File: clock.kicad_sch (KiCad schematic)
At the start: 52 parts, among them J1 USB_C_Receptacle_USB2.0_16P, J3 Conn_01x02_Pin, J4 Conn_01x02_Pin, J5 Battery, Q1 2N7002K, Q2 NPN, SW1 SW_SPST, SW2 SW_SPST, SW4 SW_SPDT, SW5 SW_SPST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

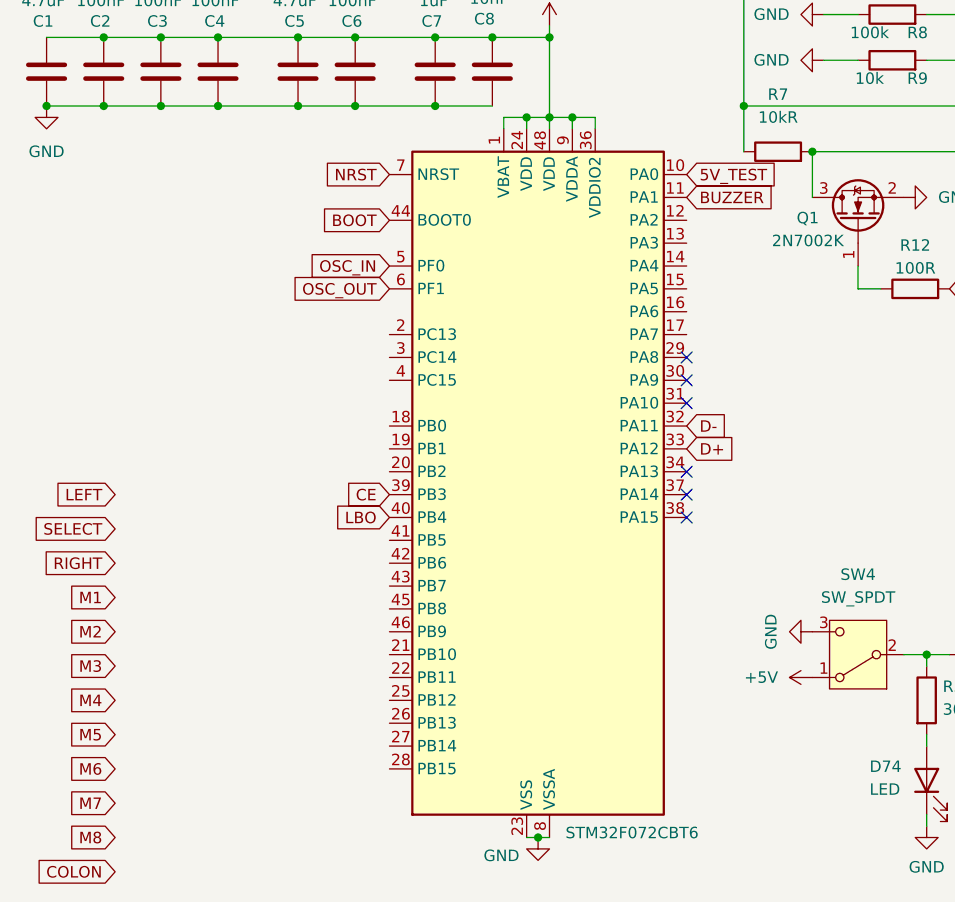
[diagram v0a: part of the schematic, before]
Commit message: all wiring done, need to clean up silk screen edge clips + double check pins for charlieplex & buttons
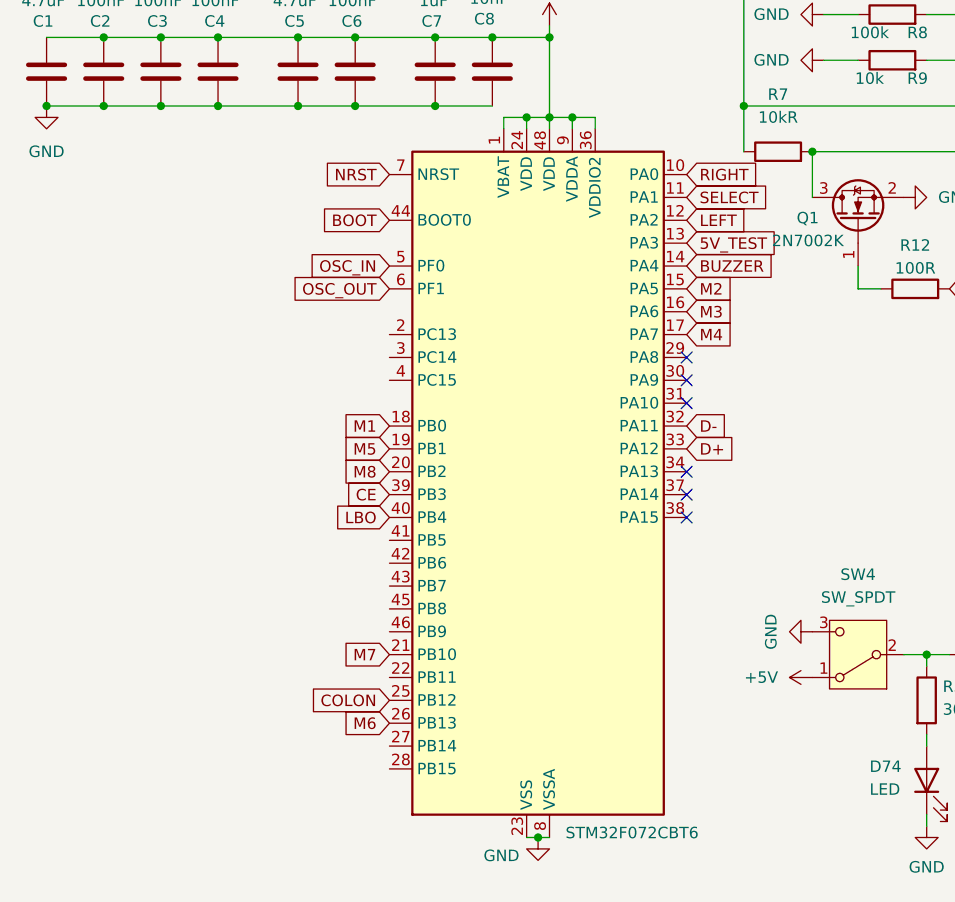
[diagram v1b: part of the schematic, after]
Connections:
- net 5V_TEST: now also U1.13 (PA3); no longer U1.10 (PA0)
- net BUZZER: now also U1.14 (PA4); no longer U1.11 (PA1)
- net COLON: now also U1.25 (PB12)
- net LEFT: now also U1.12 (PA2)
- net M1: now also U1.18 (PB0)
- net M2: now also U1.15 (PA5)
- net M3: now also U1.16 (PA6)
- net M4: now also U1.17 (PA7)
- net M5: now also U1.19 (PB1)
- net M6: now also U1.26 (PB13)
- net M7: now also U1.21 (PB10)
- net M8: now also U1.20 (PB2)
- net RIGHT: now also U1.10 (PA0)
- net SELECT: now also U1.11 (PA1)
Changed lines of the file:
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@@
 	(label "BAT"
 		(at 162.56 90.17 0)
-		(fields_autoplaced yes)
 		(effects
 			(font
@@
 	(label "VBUS"
 		(at 49.53 29.21 0)
-		(fields_autoplaced yes)
 		(effects
 			(font
@@
 	(global_label "RIGHT"
 		(shape input)
-		(at 24.13 158.75 180)
-		(fields_autoplaced yes)
-		(effects
-			(font
-				(size 1.27 1.27)
-			)
-			(justify right)
-		)
-		(property "Intersheetrefs" "${INTERSHEET_REFS}"
-			(at 15.7019 158.75 0)
-			(effects
-				(font
-					(size 1.27 1.27)
-				)
-				(justify right)
+		(at 87.63 115.57 0)
+		(fields_autoplaced yes)
+		(effects
+			(font
+				(size 1.27 1.27)
+			)
+			(justify left)
+		)
+		(property "Intersheetrefs" "${INTERSHEET_REFS}"
+			(at 96.0581 115.57 0)
+			(effects
+				(font
+					(size 1.27 1.27)
+				)
+				(justify left)
 				(hide yes)
 			)
@@
 	(global_label "5V_TEST"
 		(shape input)
-		(at 87.63 115.57 0)
-		(fields_autoplaced yes)
-		(effects
-			(font
-				(size 1.27 1.27)
-			)
-			(justify left)
-		)
-		(property "Intersheetrefs" "${INTERSHEET_REFS}"
-			(at 98.1746 115.57 0)
+		(at 87.63 123.19 0)
+		(fields_autoplaced yes)
+		(effects
+			(font
+				(size 1.27 1.27)
+			)
+			(justify left)
+		)
+		(property "Intersheetrefs" "${INTERSHEET_REFS}"
+			(at 98.1746 123.19 0)
 			(effects
 				(font
@@
 	(global_label "SELECT"
 		(shape input)
-		(at 24.13 154.94 180)
-		(fields_autoplaced yes)
-		(effects
-			(font
-				(size 1.27 1.27)
-			)
-			(justify right)
-		)
-		(property "Intersheetrefs" "${INTERSHEET_REFS}"
-			(at 14.3716 154.94 0)
-			(effects
-				(font
-					(size 1.27 1.27)
-				)
-				(justify right)
+		(at 87.63 118.11 0)
+		(fields_autoplaced yes)
+		(effects
+			(font
+				(size 1.27 1.27)
+			)
+			(justify left)
+		)
+		(property "Intersheetrefs" "${INTERSHEET_REFS}"
+			(at 97.3884 118.11 0)
+			(effects
+				(font
+					(size 1.27 1.27)
+				)
+				(justify left)
 				(hide yes)
 			)
@@
 	(global_label "LEFT"
 		(shape input)
-		(at 24.13 151.13 180)
-		(fields_autoplaced yes)
-		(effects
-			(font
-				(size 1.27 1.27)
-			)
-			(justify right)
-		)
-		(property "Intersheetrefs" "${INTERSHEET_REFS}"
-			(at 16.9115 151.13 0)
-			(effects
-				(font
-					(size 1.27 1.27)
-				)
-				(justify right)
+		(at 87.63 120.65 0)
+		(fields_autoplaced yes)
+		(effects
+			(font
+				(size 1.27 1.27)
+			)
+			(justify left)
+		)
+		(property "Intersheetrefs" "${INTERSHEET_REFS}"
+			(at 94.8485 120.65 0)
+			(effects
+				(font
+					(size 1.27 1.27)
+				)
+				(justify left)
 				(hide yes)
 			)
@@
 	(global_label "M4"
 		(shape input)
-		(at 24.13 173.99 180)
-		(fields_autoplaced yes)
-		(effects
-			(font
-				(size 1.27 1.27)
-			)
-			(justify right)
-		)
-		(property "Intersheetrefs" "${INTERSHEET_REFS}"
-			(at 18.4839 173.99 0)
-			(effects
-				(font
-					(size 1.27 1.27)
-				)
-				(justify right)
+		(at 87.63 133.35 0)
+		(fields_autoplaced yes)
+		(effects
+			(font
+				(size 1.27 1.27)
+			)
+			(justify left)
+		)
+		(property "Intersheetrefs" "${INTERSHEET_REFS}"
+			(at 93.2761 133.35 0)
+			(effects
+				(font
+					(size 1.27 1.27)
+				)
+				(justify left)
 				(hide yes)
 			)
@@
 	(global_label "M6"
 		(shape input)
-		(at 24.13 181.61 180)
-		(fields_autoplaced yes)
-		(effects
-			(font
-				(size 1.27 1.27)
-			)
-			(justify right)
-		)
-		(property "Intersheetrefs" "${INTERSHEET_REFS}"
-			(at 18.4839 181.61 0)
+		(at 54.61 176.53 180)
+		(fields_autoplaced yes)
+		(effects
+			(font
+				(size 1.27 1.27)
+			)
+			(justify right)
+		)
+		(property "Intersheetrefs" "${INTERSHEET_REFS}"
+			(at 48.9639 176.53 0)
 			(effects
 				(font
@@
 	(global_label "COLON"
 		(shape input)
-		(at 24.13 193.04 180)
-		(fields_autoplaced yes)
-		(effects
-			(font
-				(size 1.27 1.27)
-			)
-			(justify right)
-		)
-		(property "Intersheetrefs" "${INTERSHEET_REFS}"
-			(at 14.8552 193.04 0)
+		(at 54.61 173.99 180)
+		(fields_autoplaced yes)
+		(effects
+			(font
+				(size 1.27 1.27)
+			)
+			(justify right)
+		)
+		(property "Intersheetrefs" "${INTERSHEET_REFS}"
+			(at 45.3352 173.99 0)
 			(effects
 				(font
@@
 	(global_label "M8"
 		(shape input)
-		(at 24.13 189.23 180)
-		(fields_autoplaced yes)
-		(effects
-			(font
-				(size 1.27 1.27)
-			)
-			(justify right)
-		)
-		(property "Intersheetrefs" "${INTERSHEET_REFS}"
-			(at 18.4839 189.23 0)
+		(at 54.61 148.59 180)
+		(fields_autoplaced yes)
+		(effects
+			(font
+				(size 1.27 1.27)
+			)
+			(justify right)
+		)
+		(property "Intersheetrefs" "${INTERSHEET_REFS}"
+			(at 48.9639 148.59 0)
 			(effects
 				(font
@@
 	(global_label "BUZZER"
 		(shape input)
-		(at 87.63 118.11 0)
-		(fields_autoplaced yes)
-		(effects
-			(font
-				(size 1.27 1.27)
-			)
-			(justify left)
-		)
-		(property "Intersheetrefs" "${INTERSHEET_REFS}"
-			(at 98.0537 118.11 0)
+		(at 87.63 125.73 0)
+		(fields_autoplaced yes)
+		(effects
+			(font
+				(size 1.27 1.27)
+			)
+			(justify left)
+		)
+		(property "Intersheetrefs" "${INTERSHEET_REFS}"
+			(at 98.0537 125.73 0)
 			(effects
 				(font
@@
 	(global_label "M2"
 		(shape input)
-		(at 24.13 166.37 180)
-		(fields_autoplaced yes)
-		(effects
-			(font
-				(size 1.27 1.27)
-			)
-			(justify right)
-		)
-		(property "Intersheetrefs" "${INTERSHEET_REFS}"
-			(at 18.4839 166.37 0)
-			(effects
-				(font
-					(size 1.27 1.27)
-				)
-				(justify right)
+		(at 87.63 128.27 0)
+		(fields_autoplaced yes)
+		(effects
+			(font
+				(size 1.27 1.27)
+			)
+			(justify left)
+		)
+		(property "Intersheetrefs" "${INTERSHEET_REFS}"
+			(at 93.2761 128.27 0)
+			(effects
+				(font
+					(size 1.27 1.27)
+				)
+				(justify left)
 				(hide yes)
 			)
@@
 	(global_label "M1"
 		(shape input)
-		(at 24.13 162.56 180)
-		(fields_autoplaced yes)
-		(effects
-			(font
-				(size 1.27 1.27)
-			)
-			(justify right)
-		)
-		(property "Intersheetrefs" "${INTERSHEET_REFS}"
-			(at 18.4839 162.56 0)
+		(at 54.61 143.51 180)
+		(fields_autoplaced yes)
+		(effects
+			(font
+				(size 1.27 1.27)
+			)
+			(justify right)
+		)
+		(property "Intersheetrefs" "${INTERSHEET_REFS}"
+			(at 48.9639 143.51 0)
 			(effects
 				(font
@@
 	(global_label "M3"
 		(shape input)
-		(at 24.13 170.18 180)
-		(fields_autoplaced yes)
-		(effects
-			(font
-				(size 1.27 1.27)
-			)
-			(justify right)
-		)
-		(property "Intersheetrefs" "${INTERSHEET_REFS}"
-			(at 18.4839 170.18 0)
-			(effects
-				(font
-					(size 1.27 1.27)
-				)
-				(justify right)
+		(at 87.63 130.81 0)
+		(fields_autoplaced yes)
+		(effects
+			(font
+				(size 1.27 1.27)
+			)
+			(justify left)
+		)
+		(property "Intersheetrefs" "${INTERSHEET_REFS}"
+			(at 93.2761 130.81 0)
+			(effects
+				(font
+					(size 1.27 1.27)
+				)
+				(justify left)
 				(hide yes)
 			)
@@
 	(global_label "M5"
 		(shape input)
-		(at 24.13 177.8 180)
-		(fields_autoplaced yes)
-		(effects
-			(font
-				(size 1.27 1.27)
-			)
-			(justify right)
-		)
-		(property "Intersheetrefs" "${INTERSHEET_REFS}"
-			(at 18.4839 177.8 0)
+		(at 54.61 146.05 180)
+		(fields_autoplaced yes)
+		(effects
+			(font
+				(size 1.27 1.27)
+			)
+			(justify right)
+		)
+		(property "Intersheetrefs" "${INTERSHEET_REFS}"
+			(at 48.9639 146.05 0)
 			(effects
 				(font
@@
 	(global_label "M7"
 		(shape input)
-		(at 24.13 185.42 180)
-		(fields_autoplaced yes)
-		(effects
-			(font
-				(size 1.27 1.27)
-			)
-			(justify right)
-		)
-		(property "Intersheetrefs" "${INTERSHEET_REFS}"
-			(at 18.4839 185.42 0)
-			(effects
-				(font
+		(at 54.61 168.91 180)
+		(fields_autoplaced yes)
+		(effects
+			(font
+				(size 1.27 1.27)
+			)
+			(justify right)
+		)
+		(property "Intersheetrefs" "${INTERSHEET_REFS}"
+			(at 48.9639 168.91 0)
+			(effects
+				(font

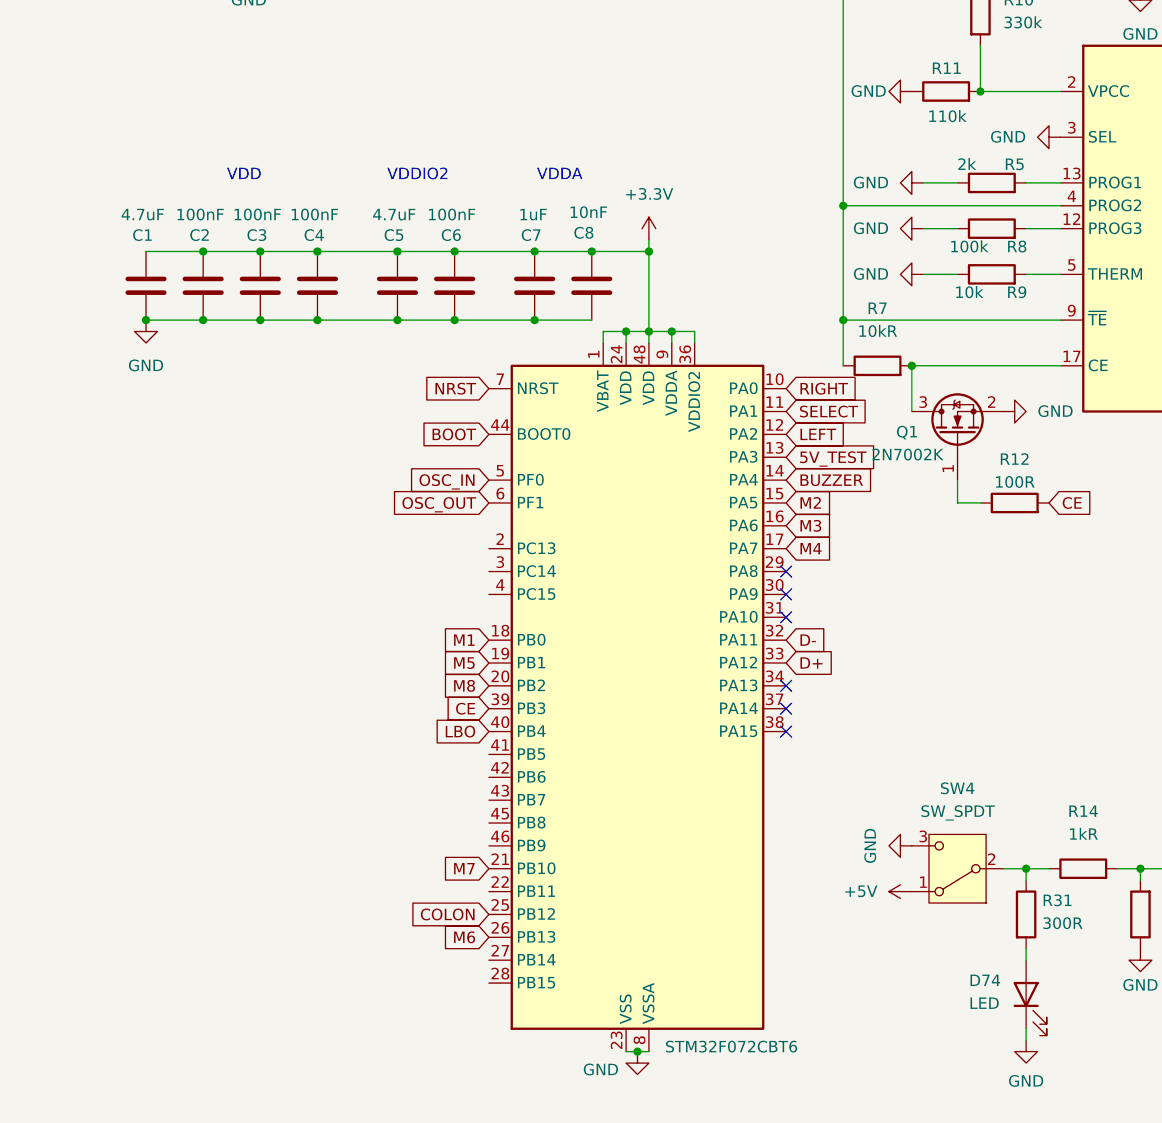
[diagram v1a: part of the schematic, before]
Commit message: swapped mosfet need to fix buzzer
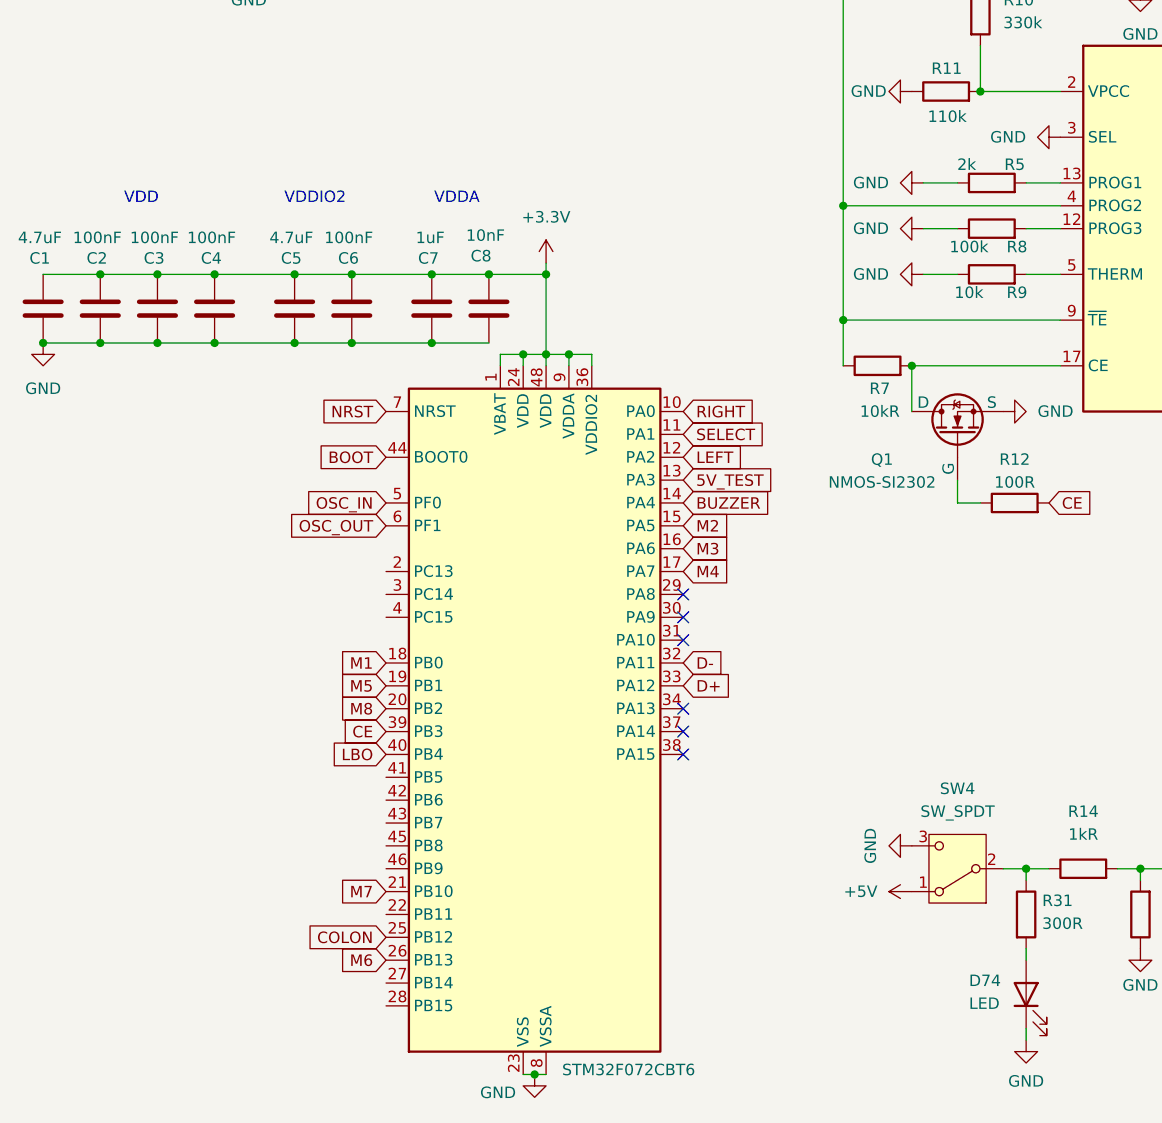
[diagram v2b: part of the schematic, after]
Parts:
- removed Q1: 2N7002K, Package_TO_SOT_SMD:SOT-23, symbol Transistor_FET:2N7002K
- added Q1: NMOS-SI2302, Package_TO_SOT_SMD:SOT-23, symbol Simulation_SPICE:NMOS
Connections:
- net GND: now also Q1.3 (S)
- net at R12.1: now also Q1.2 (G)
- net at R7.2, U4.17 (CE): now also Q1.1 (D)
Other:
- moved on the sheet: C1, C2, C3, C4, C5, C6, C7, C8

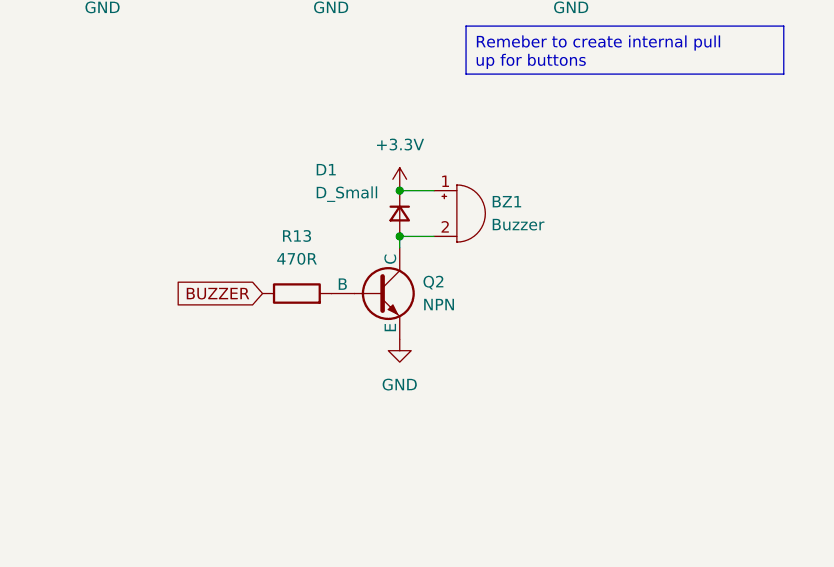
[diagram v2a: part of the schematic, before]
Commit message: beginning buzzer changes
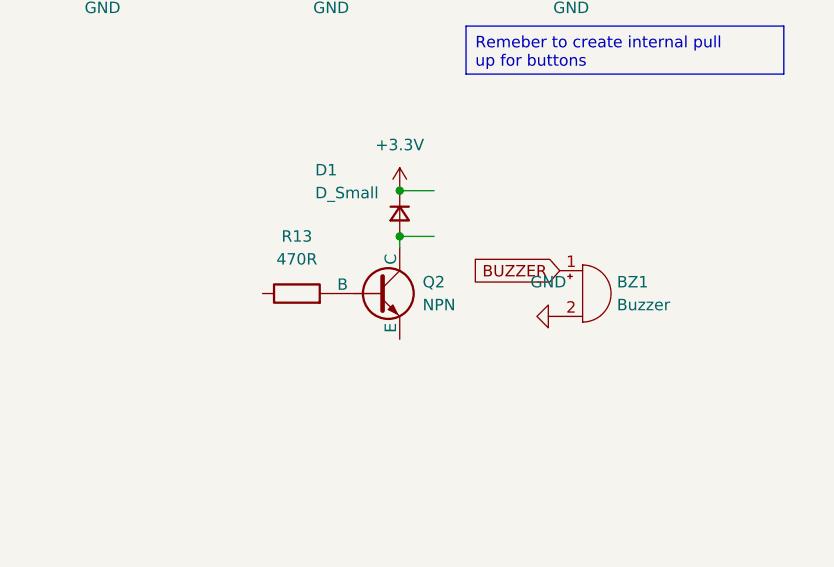
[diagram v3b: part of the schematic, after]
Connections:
- net +3.3V: no longer BZ1.1 (+)
- net BUZZER: now also BZ1.1 (+); no longer R13.1
- net GND: now also BZ1.2 (-); no longer Q2.3 (E)
- net at D1.2 (A), Q2.1 (C): no longer BZ1.2 (-)
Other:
- moved on the sheet: BZ1
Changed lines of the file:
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@@
 	(label "BAT"
 		(at 162.56 90.17 0)
+		(fields_autoplaced yes)
 		(effects
 			(font
@@
 	(label "VBUS"
 		(at 49.53 29.21 0)
+		(fields_autoplaced yes)
 		(effects
 			(font
@@
 	(global_label "BUZZER"
 		(shape input)
-		(at 224.79 90.17 180)
+		(at 257.81 87.63 180)
 		(fields_autoplaced yes)
 		(effects
@@
 		)
 		(property "Intersheetrefs" "${INTERSHEET_REFS}"
-			(at 214.3663 90.17 0)
+			(at 247.3863 87.63 0)
 			(effects
 				(font
@@
 	(symbol
 		(lib_id "Device:Buzzer")
-		(at 246.38 81.28 0)
+		(at 260.35 90.17 0)
 		(unit 1)
 		(exclude_from_sim no)
@@
 		(fields_autoplaced yes)
 		(property "Reference" "BZ1"
-			(at 250.19 80.0099 0)
+			(at 264.16 88.8999 0)
 			(effects
 				(font
@@
 		)
 		(property "Value" "Buzzer"
-			(at 250.19 82.5499 0)
+			(at 264.16 91.4399 0)
 			(effects
 				(font
@@
 		)
 		(property "Footprint" "Buzzer_Beeper:MagneticBuzzer_CUI_CMT-8504-100-SMT"
-			(at 245.745 78.74 90)
+			(at 259.715 87.63 90)
 			(effects
 				(font
@@
 		)
 		(property "Datasheet" "~"
-			(at 245.745 78.74 90)
+			(at 259.715 87.63 90)
 			(effects
 				(font
@@
 		)
 		(property "Description" "Buzzer, polarized"
-			(at 246.38 81.28 0)
+			(at 260.35 90.17 0)
 			(effects
 				(font
@@
 	(symbol
 		(lib_id "power:GND")
-		(at 240.03 95.25 0)
+		(at 257.81 92.71 270)
 		(unit 1)
 		(exclude_from_sim no)
@@
 		(fields_autoplaced yes)
 		(property "Reference" "#PWR09"
-			(at 240.03 101.6 0)
+			(at 251.46 92.71 0)
 			(effects
 				(font
@@
 		)
 		(property "Value" "GND"
-			(at 240.03 100.33 0)
+			(at 256.54 88.9 90)
 			(effects
 				(font
@@
 		)
 		(property "Footprint" ""
-			(at 240.03 95.25 0)
+			(at 257.81 92.71 0)
 			(effects
 				(font
@@
 		)
 		(property "Datasheet" ""
-			(at 240.03 95.25 0)
+			(at 257.81 92.71 0)
 			(effects
 				(font
@@
 		)
 		(property "Description" "Power symbol creates a global label with name \"GND\" , ground"
-			(at 240.03 95.25 0)
+			(at 257.81 92.71 0)
 			(effects
 				(font
